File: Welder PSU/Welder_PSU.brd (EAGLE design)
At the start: 380 x 200 mm, 216 parts, among them IC101 UCC28951PWR, IC102 UCC21542DWK, IC103 UCC21542DWK, IC104 UCC27524DGNVSS, IC105 MCP6001UT, IC106 UCC27524DGNVSS, IC107 MCP6001UT, IC108 MCP6001UT, IC201 NCP1014AP065G, IC202 AP63301WU-7, IC203 LD1117S33TR, IC204 LM317AEMP, J301 TE_282841-2TE_282841-2_0_0, J401 TE_282841-2TE_282841-2_0_0, K301 PANASONIC_ALFG2PF09PANASONIC_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, Q101 BSS123TA, Q201 PS2501L-1-ARENESAS_ELECTRONIC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, T101 SIHG039N60EF, T102 SIHG039N60EF, T103 SIHG039N60EF, T104 SIHG039N60EF, T105 SIHG039N60EF, T106 SIHG039N60EF, T107 SIHG039N60EF, T108 SIHG039N60EF, U201 TL431AQDBZR,215NEXPERIA_TL431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, X1 726386-2TE_726386-2, X103 726386-2TE_726386-2, X104 726386-2TE_726386-2, X2 726386-2TE_726386-2, X3 7461061, X4 7461061

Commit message: V00.00 Changes
Working on Layout
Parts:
- moved R151 129.6 mm to (210.2, 15.2)
- moved R152 129.5 mm to (210.2, 4.45)
- moved R154 128.9 mm to (203.8, 4.45), turned to 180 degrees
- moved R153 127.7 mm to (203.8, 15.2), turned to 180 degrees
- moved R156 125.1 mm to (199.4, 15.2)
- moved C129 120.7 mm to (208.9, 8.26), turned to 90 degrees
- moved C130 120.5 mm to (208.9, 12.1)
- moved C131 120.1 mm to (205.7, 10.2)
- moved R134 117.6 mm to (364.6, 176.9)
- moved C137 117.5 mm to (179.1, 8.89), turned to 90 degrees
- moved R158 116.9 mm to (189.9, 4.45)
- moved R155 114.9 mm to (200.0, 4.45)
- moved C133 113.8 mm to (201.3, 6.99), turned to 180 degrees
- moved T104 112.6 mm to (363.2, 182.9)
- moved R133 112.2 mm to (358.8, 172.1), turned to 180 degrees
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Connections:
- net N$10 renamed V_RECT_F_PLUS
- net N$7 renamed WELD+
- net N$8 renamed WELD-
- removed net 10_PSFB_CONVERTER:GND: C101.2, C104.1, C105.1, C106.2, C107.1, C108.1, C111.1, C112.1, C113.1, C114.1, C117.1, C118.1, C121.2, C122.1, C123.2, C124.1, C125.1, C126.1, C127.1, C128.1, C131.1, C132.1, C133.2, C135.2, C136.2, C139.2, C140.2, IC101.24, IC102.4, IC103.4, IC104.3, IC105.2, IC106.3, IC107.2, IC108.2, Q101.2, R101.2, R103.1, R104.1, R105.1, R107.1, R109.1, R110.1, R111.2, R112.2, R117.1, R119.2, R120.2, R136.2, R137.2, R149.1, R152.2, R156.1, R163.1, R167.2, R199.1, T105.3, T106.3, T107.3, T108.3, TR101.2
- removed net 10_PSFB_CONVERTER:N_OUTE_2: R142.2
- removed net 10_PSFB_CONVERTER:N_OUTF_2: R146.2
- new net 10_PSFB_CONVERTER:N$40: R110.1
- new net 10_PSFB_CONVERTER:N$45: R101.2
- new net 10_PSFB_CONVERTER:N$53: R103.1, R104.1, R105.1
- new net 10_PSFB_CONVERTER:N$62: C101.2
- new net 10_PSFB_CONVERTER:N$65: C104.1
- new net 10_PSFB_CONVERTER:N$66: IC105.2
- new net 10_PSFB_CONVERTER:N$67: R119.2
- new net 10_PSFB_CONVERTER:N$68: IC102.4
- new net 10_PSFB_CONVERTER:N$69: C112.1
- new net 10_PSFB_CONVERTER:N$70: C118.1
- new net 10_PSFB_CONVERTER:N$71: C117.1
- new net 10_PSFB_CONVERTER:N$72: R136.2
- new net 10_PSFB_CONVERTER:N$73: C139.2
- new net 10_PSFB_CONVERTER:VSEC2-: R147.1, R148.1, T107.2, T108.2, TR102.6
- new net 10_PSFB_CONVERTER:V_SEC1+: R143.1, R144.1, T105.2, T106.2, TR102.3
- new net GND1: C105.1, C106.2, C107.1, C108.1, C111.1, C113.1, C114.1, C121.2, C122.1, C123.2, C124.1, C125.1, C126.1, C131.1, C132.1, C133.2, C135.2, C136.2, C140.2, IC101.24, IC103.4, IC104.3, IC106.3, IC107.2, IC108.2, Q101.2, R111.2, R112.2, R117.1, R120.2, R137.2, R149.1, R152.2, R156.1, R163.1, R167.2, R199.1, T105.3, T106.3, T107.3, TR101.2
- net 10_PSFB_CONVERTER:AN_OUTE_2: now also R142.2
- net 10_PSFB_CONVERTER:AN_OUTF_2: now also R146.2
- net 10_PSFB_CONVERTER:N$1: now also R107.1, R109.1; no longer R143.1, R144.1, T105.2, T106.2, TR102.3
- net 10_PSFB_CONVERTER:N$39: now also C127.1, C128.1, T108.3; no longer R147.1, R148.1, T107.2, T108.2, TR102.6
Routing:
- net 10_PSFB_CONVERTER:VSS_C: track 4.59 -> 449.5 mm, vias 0 -> 2
- net V_RECT_F_PLUS: track 12.4 -> 372.8 mm
- net 10_PSFB_CONVERTER:VSS_A: track 4.66 -> 340.5 mm, vias 0 -> 17
- net 10_PSFB_CONVERTER:AN_OUTD: track 10.7 -> 294.4 mm, vias 1 -> 0
- net 10_PSFB_CONVERTER:AN_OUTC: track 11.6 -> 273.3 mm, vias 1 -> 0
- net 10_PSFB_CONVERTER:AN_OUTB: track 10.5 -> 255.7 mm, vias 1 -> 0
- net GND2: track 146.8 -> 389.7 mm
- net 10_PSFB_CONVERTER:AN_OUTA: track 12.4 -> 237.4 mm, vias 1 -> 0
- net 10_PSFB_CONVERTER:AN_OUTE_2: track 0.00 -> 185.0 mm, vias 0 -> 2
- net GND1: track 0.00 -> 167.4 mm, vias 0 -> 92
- net WELD-: track 0.00 -> 164.3 mm, vias 0 -> 2
- net WELD+: track 0.00 -> 150.6 mm
- net 10_PSFB_CONVERTER:AN_OUTE_1: track 0.00 -> 146.0 mm, vias 0 -> 2
- net 10_PSFB_CONVERTER:N$19: track 133.8 -> 15.0 mm
- net 10_PSFB_CONVERTER:VSEC2-: track 0.00 -> 116.5 mm, vias 0 -> 207
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- added copper zone on layer 1, net 10_PSFB_CONVERTER:N$20
- added copper zone on layer 1, net 10_PSFB_CONVERTER:N$46
- added copper zone on layer 1, net 10_PSFB_CONVERTER:VSEC2-
- added copper zone on layer 16, net 10_PSFB_CONVERTER:VSEC2-
- added copper zone on layer 1, net 10_PSFB_CONVERTER:VSS_A
- added copper zone on layer 16, net 10_PSFB_CONVERTER:VSS_A
- added copper zone on layer 1, net 10_PSFB_CONVERTER:VSS_C
- added copper zone on layer 16, net 10_PSFB_CONVERTER:VSS_C
- added copper zone on layer 1, net 10_PSFB_CONVERTER:V_SEC1+
- added copper zone on layer 16, net 10_PSFB_CONVERTER:V_SEC1+
- added copper zone on layer 1, net GND1
- added copper zone on layer 16, net GND1
- added copper zone on layer 16, net GND2
- added copper zone on layer 1, net V_RECT_F_PLUS
- added copper zone on layer 1, net WELD+
- added copper zone on layer 16, net WELD+
- added copper zone on layer 1, net WELD-
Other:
- board size 380 x 200 mm -> 380 x 210 mm

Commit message: V00.00
Modifying Layout
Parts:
- moved J301 129.0 mm to (179.1, 127.0)
- moved R154 12.1 mm to (200.3, 16.0)
- moved R152 11.4 mm to (210.3, 15.9)
- moved C131 7.55 mm to (213.0, 12.3), turned to 270 degrees
- moved R155 6.94 mm to (196.1, 10.2), turned to 90 degrees
- moved R151 5.84 mm to (210.3, 9.40)
- moved R157 5.80 mm to (193.9, 10.2), turned to 270 degrees
- moved R158 5.73 mm to (189.5, 10.2), turned to 90 degrees
- moved C129 5.64 mm to (210.3, 13.7), turned to 0 degrees
- moved C136 5.60 mm to (154.4, 5.97)
- moved C138 5.60 mm to (176.0, 8.51)
- moved R164 5.60 mm to (144.3, 5.97)
- moved J401 5.60 mm to (127.5, 4.57)
- moved 47K100 5.60 mm to (151.9, 5.97)
- moved C135 5.60 mm to (149.4, 5.97)
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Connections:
- net N$4 renamed V_12V
- net N$5 renamed V_5V0
- net N$6 renamed V_3V3
- removed net 10_PSFB_CONVERTER:N$1: R107.1, R109.1
- removed net 10_PSFB_CONVERTER:N$40: R110.1
- removed net 10_PSFB_CONVERTER:N$45: R101.2
- removed net 10_PSFB_CONVERTER:N$53: R103.1, R104.1, R105.1
- removed net 10_PSFB_CONVERTER:N$62: C101.2
- removed net 10_PSFB_CONVERTER:N$65: C104.1
- removed net 10_PSFB_CONVERTER:N$66: IC105.2
- removed net 10_PSFB_CONVERTER:N$67: R119.2
- removed net 10_PSFB_CONVERTER:N$68: IC102.4
- removed net 10_PSFB_CONVERTER:N$69: C112.1
- removed net 10_PSFB_CONVERTER:N$70: C118.1
- removed net 10_PSFB_CONVERTER:N$71: C117.1
- removed net 10_PSFB_CONVERTER:N$72: R136.2
- removed net 10_PSFB_CONVERTER:N$73: C139.2
- removed net FLYBACK1:GND: C201.2, C202.2, C204.1, C206.2, C207.2, C208.2, C215.2, C216.2, C217.2, C218.2, IC202.4, IC203.1, R202.1, R205.1, R206.1, R209.1, TR201.1, U201.3
- removed net GND1: C105.1, C106.2, C107.1, C108.1, C111.1, C113.1, C114.1, C121.2, C122.1, C123.2, C124.1, C125.1, C126.1, C131.1, C132.1, C133.2, C135.2, C136.2, C140.2, IC101.24, IC103.4, IC104.3, IC106.3, IC107.2, IC108.2, Q101.2, R111.2, R112.2, R117.1, R120.2, R137.2, R149.1, R152.2, R156.1, R163.1, R167.2, R199.1, T105.3, T106.3, T107.3, TR101.2
- new net 10_PSFB_CONVERTER:GND_A: C125.1, C126.1, T106.3
- new net MCU1:GND: J401.2
- net GND: now also C101.2, C104.1, C105.1, C106.2, C107.1, C108.1, C111.1, C112.1, C113.1, C114.1, C117.1, C118.1, C121.2, C122.1, C123.2, C124.1, C131.1, C132.1, C133.2, C135.2, C136.2, C139.2, C140.2, C201.2, C202.2, C204.1, C206.2, C207.2, C208.2, C215.2, C216.2, C217.2, C218.2, IC101.24, IC102.4, IC103.4, IC104.3, IC105.2, IC106.3, IC107.2, IC108.2, IC202.4, IC203.1, Q101.2, R101.2, R103.1, R104.1, R105.1, R107.1, R109.1, R110.1, R111.2, R112.2, R117.1, R119.2, R120.2, R136.2, R137.2, R149.1, R152.2, R156.1, R163.1, R167.2, R199.1, R202.1, R205.1, R206.1, R209.1, TR101.2, TR201.1, U201.3; no longer J401.2
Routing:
- net GND: track 14.3 -> 368.8 mm, vias 0 -> 98
- net V_3V3: track 160.9 -> 500.3 mm, vias 3 -> 7
- net V_12V: track 109.8 -> 441.0 mm, vias 0 -> 3
- net GND2: track 389.7 -> 712.4 mm, vias 0 -> 2
- net GND1: track 167.4 -> 0.00 mm, vias 92 -> 0
- net 10_PSFB_CONVERTER:N$19: track 15.0 -> 119.4 mm
- net WELD+: track 150.6 -> 253.1 mm, vias 0 -> 2
- net 10_PSFB_CONVERTER:EA_IN: track 9.35 -> 100.3 mm, vias 0 -> 2
- net V_5V0: track 63.1 -> 145.7 mm, vias 0 -> 2
- net FLYBACK1:GND: track 56.6 -> 0.00 mm
- net 10_PSFB_CONVERTER:N$60: track 0.00 -> 30.8 mm
- net 10_PSFB_CONVERTER:N$11: track 0.00 -> 30.3 mm, vias 0 -> 1
- net 10_PSFB_CONVERTER:CMOS_OUTF: track 109.2 -> 127.4 mm
- net 10_PSFB_CONVERTER:N$63: track 0.00 -> 15.3 mm
- net 10_PSFB_CONVERTER:CMOS_OUTE: track 106.4 -> 118.6 mm
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- added copper zone on layer 1, net GND
- added copper zone on layer 16, net GND
- added copper zone on layer 1, net V_3V3
- removed copper zone on layer 1, net GND1
- removed copper zone on layer 16, net GND1

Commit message: V00.00
Layout Ongoing
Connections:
- removed net 10_PSFB_CONVERTER:GND_A: C125.1, C126.1, T106.3
- removed net 10_PSFB_CONVERTER:N$39: C127.1, C128.1, T108.3
- new net 30_MAINS_INPUT_PFC1:N$3: D301.1, J301.1, K301.2
- net GND: now also C125.1, C126.1, C127.1, C128.1, T105.3, T106.3, T107.3, T108.3
- net V_12V: no longer D301.1, J301.1, K301.2
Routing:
- net 30_MAINS_INPUT_PFC1:N$3: track 0.00 -> 121.5 mm
- net V_12V: track 441.0 -> 319.5 mm
- net MAINS_N: track 83.1 -> 134.7 mm, vias 0 -> 1
- net GND: track 368.8 -> 409.4 mm, vias 98 -> 293
- net 30_MAINS_INPUT_PFC1:N$2: track 27.5 -> 47.4 mm
- net MAINS_L: track 51.6 -> 68.9 mm
- net 12V_AUX: track 107.4 -> 118.3 mm
- net 10_PSFB_CONVERTER:N$9: track 4.62 -> 13.1 mm
- net 10_PSFB_CONVERTER:N$7: track 7.75 -> 10.0 mm
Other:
- board size 380 x 210 mm -> 382 x 220 mm

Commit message: V00.00 changes
Layout Ongoing
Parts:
- moved D101 0.41 mm to (192.9, 94.9), turned to 180 degrees
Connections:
- removed net 10_PSFB_CONVERTER:GND2: C119.2, C120.2
- net GND2: now also C119.2, C120.2
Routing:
- net GND2: track 712.4 -> 729.7 mm, vias 2 -> 3
- net WELD+: track 253.1 -> 269.6 mm
- net WELD-: track 169.2 -> 184.6 mm
- net 12V_AUX: track 118.3 -> 129.3 mm
- net 10_PSFB_CONVERTER:N$36: track 0.00 -> 4.21 mm
- net 10_PSFB_CONVERTER:N$11: track 30.3 -> 33.1 mm
- net 10_PSFB_CONVERTER:N$12: track 7.58 -> 10.1 mm
- net GND: track 409.4 -> 409.3 mm, vias 293 -> 294
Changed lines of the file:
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@@
 <attribute name="VOLTAGE_RATING" value="800V" x="23.495" y="168.275" size="1.778" layer="27" rot="R90" display="off"/>
 </element>
-<element name="D101" library="3D_MIG_Controller" package="SMA-DIODE" value="1A/40V/500mV" x="192.8429375" y="95.25" smashed="yes" rot="R270">
-<attribute name="NAME" x="194.7479375" y="95.25" size="0.508" layer="25" font="vector" ratio="14" rot="R270" align="bottom-center"/>
-<attribute name="PROD_ID" value="DIO-08053" x="192.8429375" y="95.25" size="1.778" layer="27" rot="R270" display="off"/>
-<attribute name="VALUE" x="192.8429375" y="95.25" size="0.381" layer="27" font="vector" ratio="10" rot="R270" align="top-center"/>
+<element name="D101" library="3D_MIG_Controller" package="SMA-DIODE" value="1A/40V/500mV" x="192.95" y="94.8570625" smashed="yes" rot="R180">
+<attribute name="NAME" x="192.95" y="92.9520625" size="0.508" layer="25" font="vector" ratio="14" rot="R180" align="bottom-center"/>
+<attribute name="PROD_ID" value="DIO-08053" x="192.95" y="94.8570625" size="1.778" layer="27" rot="R180" display="off"/>
+<attribute name="VALUE" x="192.95" y="94.8570625" size="0.381" layer="27" font="vector" ratio="10" rot="R180" align="top-center"/>
 </element>
 <element name="D102" library="3D_MIG_Controller" package="SMA-DIODE" value="MURA160T3" x="88.011" y="103.505" smashed="yes" rot="R270">
@@
 <wire x1="196.088" y1="14.439" x2="196.088" y2="17.653" width="0.254" layer="1"/>
 <wire x1="196.088" y1="17.653" x2="197.485" y2="19.05" width="0.254" layer="1"/>
-<wire x1="365.125" y1="67.822609375" x2="373.983846875" y2="62.825" width="0" layer="19" extent="1-1"/>
+<wire x1="373.983846875" y1="62.825" x2="373.983846875" y2="77.438846875" width="2.54" layer="1"/>
+<wire x1="373.983846875" y1="77.438846875" x2="375.285" y2="78.74" width="2.54" layer="1"/>
 <wire x1="360.045" y1="67.822609375" x2="365.125" y2="67.822609375" width="0" layer="19" extent="1-1"/>
-<wire x1="365.125" y1="78.74" x2="365.125" y2="67.822609375" width="0" layer="19" extent="1-1"/>
+<wire x1="373.983846875" y1="62.825" x2="365.125" y2="67.822609375" width="0" layer="19" extent="1-1"/>
 </signal>
 <signal name="WELD-">
@@
 <wire x1="213.487" y1="9.652" x2="214.63" y2="10.795" width="0.254" layer="1"/>
 <wire x1="214.63" y1="10.795" x2="214.63" y2="15.24" width="0.254" layer="1"/>
-<wire x1="365.125" y1="53.3036375" x2="372.383846875" y2="57.825" width="0" layer="19" extent="1-1"/>
+<wire x1="372.383846875" y1="57.825" x2="372.383846875" y2="42.906153125" width="2.54" layer="1"/>
+<wire x1="372.383846875" y1="42.906153125" x2="372.745" y2="42.545" width="2.54" layer="1"/>
 <wire x1="360.045" y1="53.3036375" x2="365.125" y2="53.3036375" width="0" layer="19" extent="1-1"/>
-<wire x1="365.125" y1="42.545" x2="365.125" y2="53.3036375" width="0" layer="19" extent="1-1"/>
+<wire x1="372.383846875" y1="57.825" x2="365.125" y2="53.3036375" width="0" layer="19" extent="1-1"/>
 </signal>
 <signal name="V_12V">
@@
 <contactref element="TR101" pad="1"/>
 <contactref element="D101" pad="A"/>
-<wire x1="193.675" y1="127" x2="193.675" y2="101.473" width="0.508" layer="16"/>
-<wire x1="193.675" y1="101.473" x2="192.786" y2="100.584" width="0.508" layer="16"/>
-<wire x1="192.786" y1="100.584" x2="192.7225" y2="100.6475" width="0.508" layer="16"/>
-<via x="192.7225" y="100.6475" extent="1-16" drill="0.35"/>
-<wire x1="192.7225" y1="100.6475" x2="192.7225" y2="97.3704375" width="0.508" layer="1"/>
-<wire x1="192.7225" y1="97.3704375" x2="192.8429375" y2="97.25" width="0.508" layer="1"/>
+<wire x1="193.675" y1="127" x2="193.675" y2="97.173" width="0.508" layer="16"/>
+<wire x1="193.675" y1="97.173" x2="193.3495" y2="96.8475" width="0.508" layer="16"/>
+<wire x1="193.2225" y1="96.8475" x2="193.3495" y2="96.8475" width="0.508" layer="16"/>
+<via x="193.2225" y="96.8475" extent="1-16" drill="0.35"/>
+<wire x1="193.2225" y1="96.8475" x2="193.2225" y2="96.5845625" width="0.508" layer="1"/>
+<wire x1="193.2225" y1="96.5845625" x2="194.95" y2="94.8570625" width="0.508" layer="1"/>
 </signal>
 <signal name="10_PSFB_CONVERTER:N$12" class="3">
@@
 <contactref element="R113" pad="2"/>
 <wire x1="193.04" y1="88.417" x2="192.8429375" y2="88.6140625" width="1.016" layer="1"/>
-<wire x1="192.8429375" y1="93.25" x2="193.04" y2="93.0529375" width="0.508" layer="1"/>
+<wire x1="190.95" y1="94.8570625" x2="193.04" y2="93.0529375" width="0.508" layer="1"/>
 <wire x1="193.04" y1="93.0529375" x2="193.04" y2="88.417" width="0.508" layer="1"/>
 <wire x1="193.04" y1="88.417" x2="193.192" y2="88.265" width="0.508" layer="1"/>
@@
 <wire x1="34.925" y1="96.52" x2="59.69" y2="96.52" width="2.54" layer="16"/>
 <wire x1="59.69" y1="96.52" x2="68.2625" y2="105.0925" width="2.54" layer="16"/>
-<wire x1="68.2625" y1="105.0925" x2="80.645" y2="117.475" width="2.54" layer="16"/>
+<wire x1="68.2625" y1="105.0925" x2="69.935" y2="106.765" width="2.54" layer="16"/>
+<wire x1="69.935" y1="106.765" x2="80.645" y2="117.475" width="2.54" layer="16"/>
 <wire x1="80.645" y1="117.475" x2="86.32" y2="117.475" width="2.54" layer="16"/>
 <wire x1="86.32" y1="117.475" x2="86.36" y2="117.435" width="2.54" layer="16"/>
@@
 <vertex x="158.75" y="116.205"/>
 </polygon>
-<wire x1="68.58" y1="115.15" x2="69.215" y2="105.41" width="0" layer="19" extent="1-16"/>
+<contactref element="C120" pad="2"/>
+<contactref element="C119" pad="2"/>
+<wire x1="103.505" y1="99.06" x2="105.16" y2="99.06" width="0.254" layer="1"/>
+<wire x1="106.553" y1="100.453" x2="106.553" y2="103.29" width="0.254" layer="1"/>
+<wire x1="105.16" y1="99.06" x2="106.553" y2="100.453" width="0.254" layer="1"/>
+<wire x1="79.659546875" y1="104.179" x2="72.521" y2="104.179" width="0.254" layer="1"/>
+<via x="69.935" y="106.765" extent="1-16" drill="0.35"/>
+<wire x1="72.521" y1="104.179" x2="69.935" y2="106.765" width="0.254" layer="1"/>
+<wire x1="69.935" y1="106.765" x2="69.215" y2="105.41" width="0" layer="19" extent="16-16"/>
 </signal>
 <signal name="10_PSFB_CONVERTER:VSS_C" class="4">
@@
 <contactref element="D107" pad="A"/>
 <contactref element="R140" pad="2"/>
-<wire x1="109.43104375" y1="105.3145" x2="109.366" y2="109.49538125" width="0" layer="19" extent="1-1"/>
+<wire x1="109.366" y1="109.49538125" x2="109.43104375" y2="109.4303375" width="0.254" layer="1"/>
+<wire x1="109.43104375" y1="109.4303375" x2="109.43104375" y2="105.3145" width="0.254" layer="1"/>
 </signal>
 <signal name="12V_AUX">
 <contactref element="R140" pad="1"/>
-<contactref element="C120" pad="1"/>
 <contactref element="R123" pad="1"/>
 <contactref element="C119" pad="1"/>
@@
 <wire x1="82.293" y1="105.8337625" x2="79.704784375" y2="105.8337625" width="0.508" layer="1"/>
 <wire x1="79.704784375" y1="105.8337625" x2="79.659546875" y2="105.879" width="0.508" layer="1"/>
-<wire x1="106.553" y1="104.99" x2="106.566" y2="109.49538125" width="0" layer="19" extent="1-1"/>
-<wire x1="100.97454375" y1="102.87" x2="106.553" y2="104.99" width="0" layer="19" extent="1-1"/>
-</signal>
-<signal name="10_PSFB_CONVERTER:GND2">
-<contactref element="C120" pad="2"/>
-<contactref element="C119" pad="2"/>
-<wire x1="79.659546875" y1="104.179" x2="106.553" y2="103.29" width="0" layer="19" extent="1-1"/>
+<wire x1="100.97454375" y1="102.87" x2="103.09454375" y2="104.99" width="0.254" layer="1"/>
+<contactref element="C120" pad="1"/>
+<wire x1="103.09454375" y1="104.99" x2="106.553" y2="104.99" width="0.254" layer="1"/>
+<wire x1="106.553" y1="104.99" x2="106.553" y2="109.48238125" width="0.254" layer="1"/>
+<wire x1="106.553" y1="109.48238125" x2="106.566" y2="109.49538125" width="0.254" layer="1"/>
 </signal>
 <signal name="10_PSFB_CONVERTER:AN_OUTE_2" class="3">
@@
 <vertex x="237.49" y="78.74"/>
 <vertex x="237.49" y="92.075"/>
-<vertex x="227.33" y="102.235"/>
-<vertex x="171.45" y="102.235"/>
-<vertex x="167.005" y="97.79"/>
+<vertex x="234.23" y="95.335"/>
+<vertex x="170.35" y="95.335"/>
+<vertex x="167.005" y="91.99"/>
 <vertex x="167.005" y="88.9"/>
 <vertex x="29.845" y="88.9"/>
@@
 <via x="223.52" y="-7.62" extent="1-16" drill="0.35"/>
 <wire x1="181.36" y1="127" x2="181.36" y2="98.94" width="0.508" layer="16"/>
-<wire x1="181.36" y1="98.94" x2="181.4" y2="98.9" width="0.508" layer="16"/>
+<via x="181.36" y="98.94" extent="1-16" drill="0.35"/>
 <wire x1="348.44666875" y1="21.4995" x2="340.873675" y2="21.375" width="0" layer="19" extent="1-1"/>
 <wire x1="24.765" y1="53.61" x2="28.26" y2="53.975" width="0" layer="19" extent="1-1"/>

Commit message: V00.00 changes
Layout ongoing
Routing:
- net WELD+: track 269.6 -> 285.6 mm
- net WELD-: track 184.6 -> 198.8 mm
- net GND: track 409.3 -> 414.9 mm
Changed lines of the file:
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@@
 <wire x1="373.983846875" y1="62.825" x2="373.983846875" y2="77.438846875" width="2.54" layer="1"/>
 <wire x1="373.983846875" y1="77.438846875" x2="375.285" y2="78.74" width="2.54" layer="1"/>
+<wire x1="360.045" y1="67.822609375" x2="368.9862375" y2="67.822609375" width="0.254" layer="1"/>
+<wire x1="368.9862375" y1="67.822609375" x2="373.983846875" y2="62.825" width="0.254" layer="1"/>
 <wire x1="360.045" y1="67.822609375" x2="365.125" y2="67.822609375" width="0" layer="19" extent="1-1"/>
-<wire x1="373.983846875" y1="62.825" x2="365.125" y2="67.822609375" width="0" layer="19" extent="1-1"/>
 </signal>
 <signal name="WELD-">
@@
 <wire x1="372.383846875" y1="57.825" x2="372.383846875" y2="42.906153125" width="2.54" layer="1"/>
 <wire x1="372.383846875" y1="42.906153125" x2="372.745" y2="42.545" width="2.54" layer="1"/>
+<wire x1="360.045" y1="53.3036375" x2="367.862484375" y2="53.3036375" width="0.254" layer="1"/>
+<wire x1="367.862484375" y1="53.3036375" x2="372.383846875" y2="57.825" width="0.254" layer="1"/>
 <wire x1="360.045" y1="53.3036375" x2="365.125" y2="53.3036375" width="0" layer="19" extent="1-1"/>
-<wire x1="372.383846875" y1="57.825" x2="365.125" y2="53.3036375" width="0" layer="19" extent="1-1"/>
 </signal>
 <signal name="V_12V">
@@
 <via x="223.52" y="-5.08" extent="1-16" drill="0.35"/>
 <via x="223.52" y="-7.62" extent="1-16" drill="0.35"/>
-<wire x1="181.36" y1="127" x2="181.36" y2="98.94" width="0.508" layer="16"/>
-<via x="181.36" y="98.94" extent="1-16" drill="0.35"/>
+<wire x1="181.36" y1="127" x2="181.36" y2="93.34" width="0.508" layer="16"/>
+<via x="181.36" y="93.34" extent="1-16" drill="0.35"/>
 <wire x1="348.44666875" y1="21.4995" x2="340.873675" y2="21.375" width="0" layer="19" extent="1-1"/>
 <wire x1="24.765" y1="53.61" x2="28.26" y2="53.975" width="0" layer="19" extent="1-1"/>

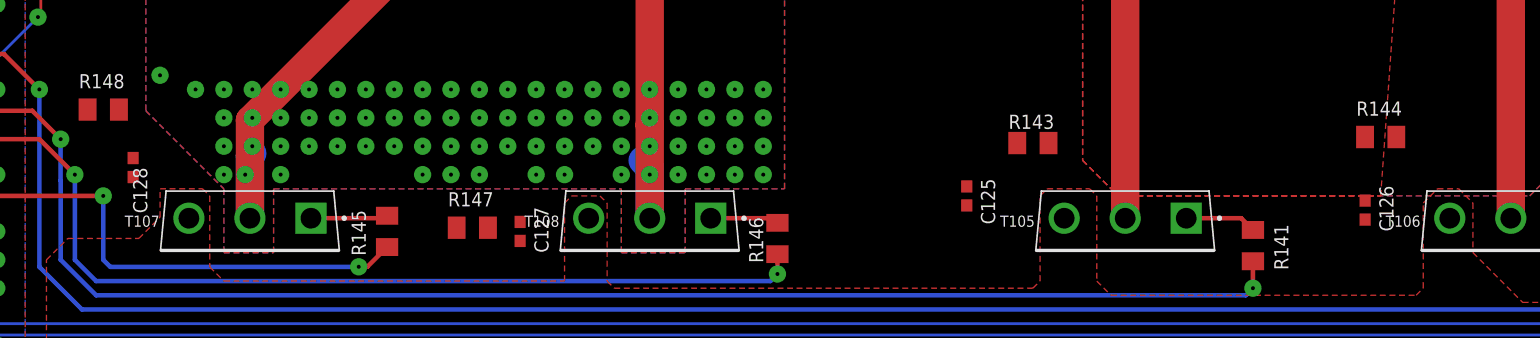
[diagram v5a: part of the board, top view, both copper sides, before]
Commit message: HW00.00
Layout Changes finalization (No Galvanic isolation of I-V measurement of secondary)
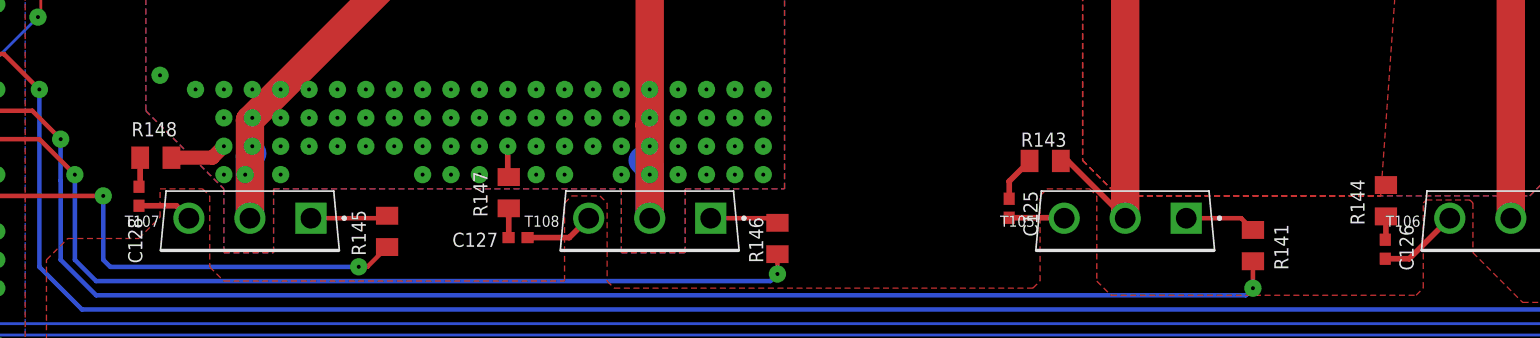
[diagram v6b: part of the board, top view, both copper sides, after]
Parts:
- moved R148 6.37 mm to (232.7, 26.9)
- moved R144 5.72 mm to (342.7, 23.1), turned to 270 degrees
- moved R147 4.53 mm to (264.2, 23.8), turned to 270 degrees
- moved C125 3.96 mm to (309.0, 22.4)
- moved C126 3.94 mm to (342.7, 18.7)
- moved C128 2.62 mm to (231.2, 23.5), turned to 90 degrees
- moved R143 1.94 mm to (312.2, 26.6)
- moved C127 0.58 mm to (265.1, 19.8), turned to 180 degrees
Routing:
- net GND: track 414.9 -> 438.2 mm
- net 10_PSFB_CONVERTER:VSEC2-: track 116.5 -> 124.4 mm
- net 10_PSFB_CONVERTER:V_SEC1+: track 103.9 -> 111.8 mm
- net 10_PSFB_CONVERTER:N$29: track 0.00 -> 4.13 mm
- net 10_PSFB_CONVERTER:N$44: track 0.00 -> 2.65 mm
- net 10_PSFB_CONVERTER:N$43: track 0.00 -> 2.63 mm
- net 10_PSFB_CONVERTER:N$37: track 0.00 -> 2.11 mm

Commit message: HW00.00
Layout finishing touches
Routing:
- net MAINS_N: track 134.7 -> 144.7 mm, vias 1 -> 0
- net MAINS_L: track 68.9 -> 72.9 mm
- added copper zone on layer 1, net 30_MAINS_INPUT_PFC1:N$1
- added copper zone on layer 1, net 30_MAINS_INPUT_PFC1:N$5
